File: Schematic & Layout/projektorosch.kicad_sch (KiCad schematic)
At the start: 18 parts

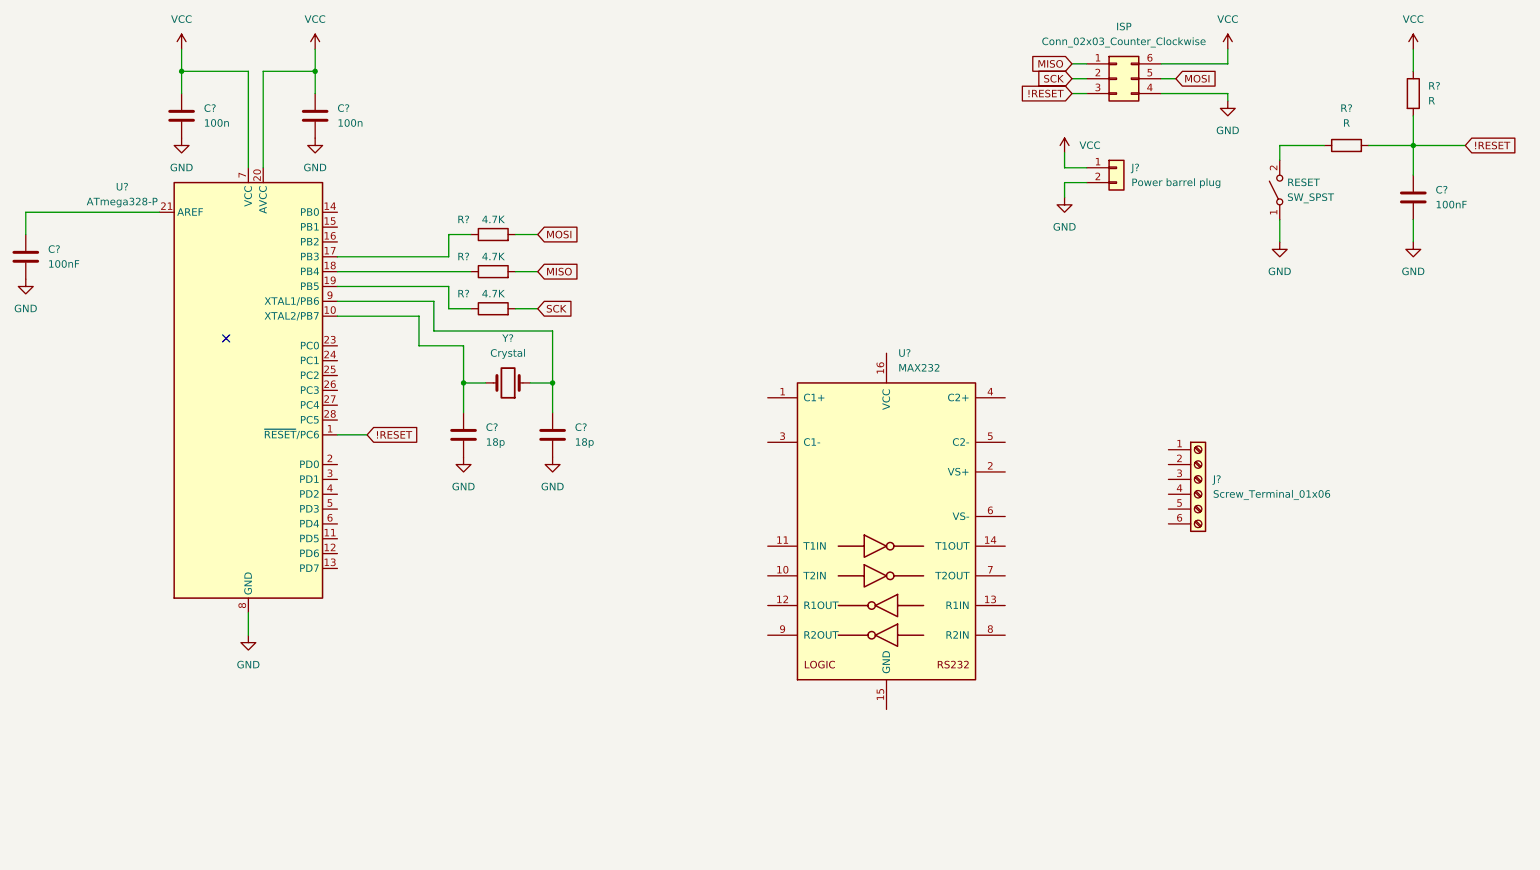
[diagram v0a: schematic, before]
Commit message: add buttons, and the connections of max232
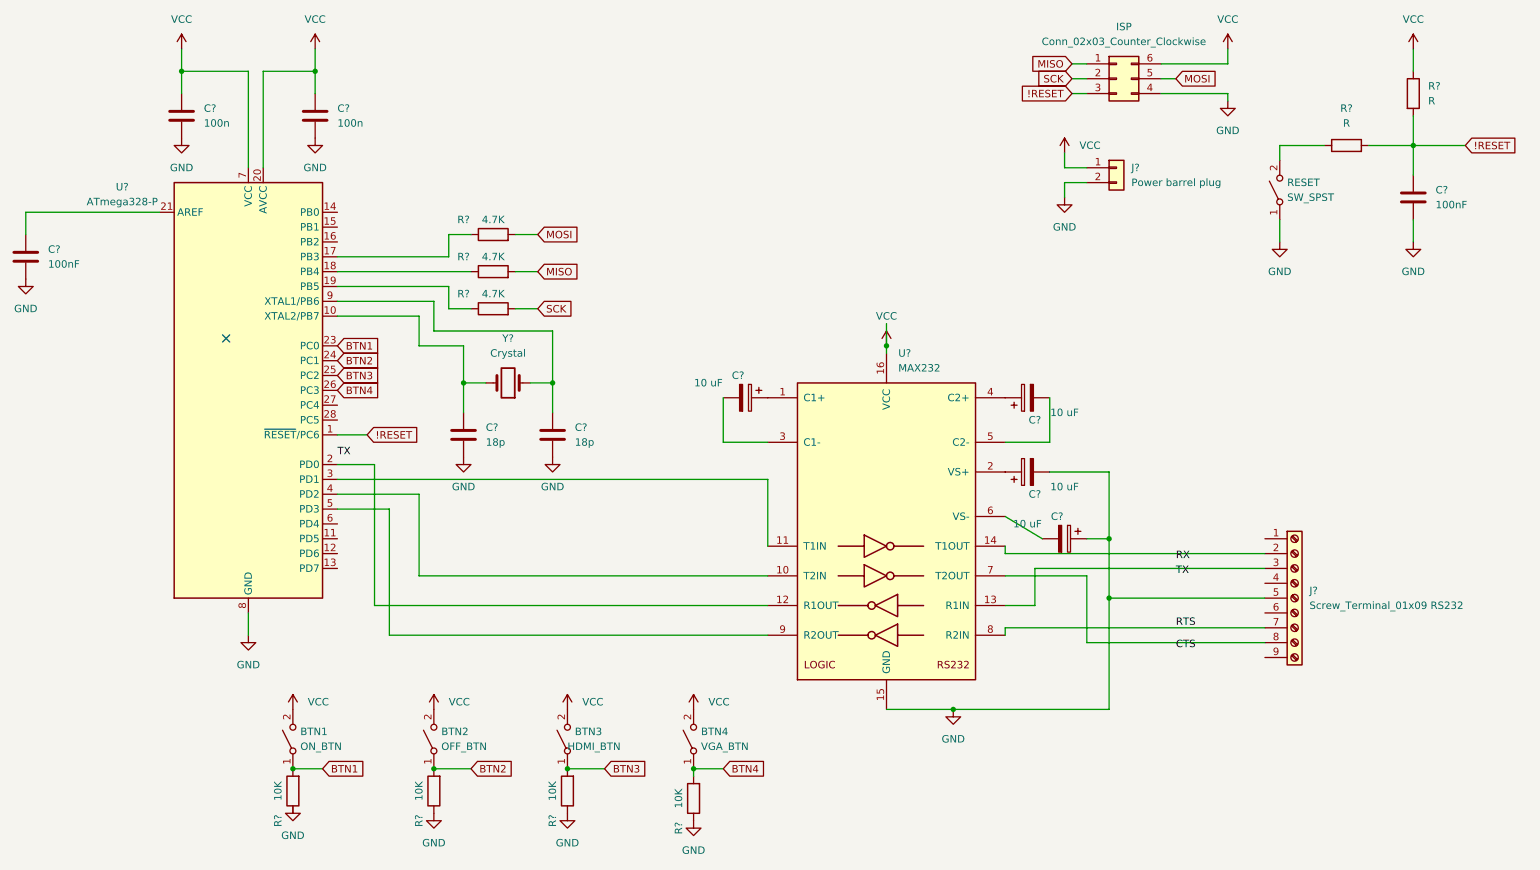
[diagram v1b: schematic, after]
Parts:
- removed J?: Screw_Terminal_01x06, Connector_Dsub:DSUB-9_Female_EdgeMount_P2.77mm, symbol Connector:Screw_Terminal_01x06
- added BTN1: ON_BTN, symbol Switch:SW_SPST
- added BTN2: OFF_BTN, symbol Switch:SW_SPST
- added BTN3: HDMI_BTN, symbol Switch:SW_SPST
- added BTN4: VGA_BTN, symbol Switch:SW_SPST
- added C? (x4): 10 uF, symbol Device:C_Polarized
- added J?: Screw_Terminal_01x09 RS232, symbol Connector:Screw_Terminal_01x09
- added R? (x4): 10K, symbol Device:R
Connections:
- net GND: now also U?.15 (GND), C?.1, C?.2, J?.5 (Pin_5), R?.1, R?.1, R?.1
- net VCC: now also U?.16 (VCC), BTN1.2 (B), BTN2.2 (B), BTN3.2 (B), BTN4.2 (B)
- net at U?.1 (C1+): now also C?.1
- net at U?.10 (T2IN): now also U?.4 (PD2)
- net at U?.11 (T1IN): now also U?.3 (PD1)
- net at U?.12 (R1OUT): now also U?.2 (PD0)
- net at U?.13 (R1IN): now also J?.3 (Pin_3)
- net at U?.14 (T1OUT): now also J?.2 (Pin_2)
- net at U?.2 (VS+): now also C?.1
- net at U?.3 (C1-): now also C?.2
- net at U?.4 (C2+): now also C?.1
- net at U?.5 (C2-): now also C?.2
- net at U?.6 (VS-): now also C?.2
- net at U?.7 (T2OUT): now also J?.8 (Pin_8)
- net RTS: now reaches U?.8 (R2IN)
- net RTS: now also J?.7 (Pin_7)
- net at U?.9 (R2OUT): now also U?.5 (PD3)
- net BTN1: now reaches U?.23 (PC0)
- net BTN1: now also BTN1.1 (A), R?.2
- net BTN2: now reaches U?.24 (PC1)
- net BTN2: now also BTN2.1 (A), R?.2
- net BTN3: now reaches U?.25 (PC2)
- net BTN3: now also BTN3.1 (A), R?.2
- net BTN4: now reaches U?.26 (PC3)
- net BTN4: now also BTN4.1 (A), R?.2

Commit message: Improvements, add overvoltage and overcurrent protection
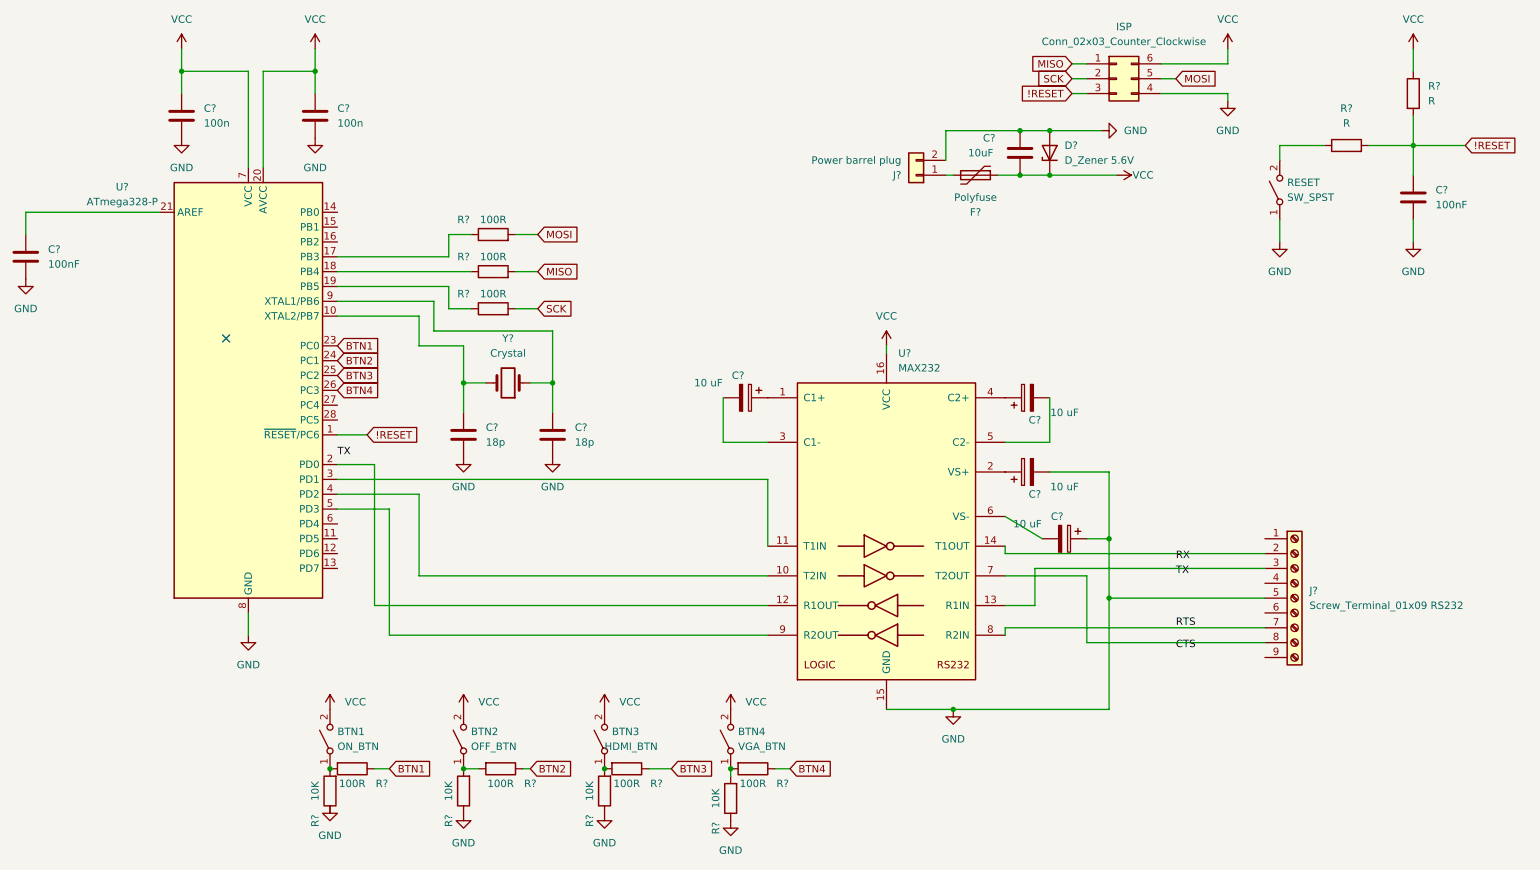
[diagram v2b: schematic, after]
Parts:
- added C?: 10uF, symbol Device:C
- added D?: D_Zener 5.6V, symbol Device:D_Zener
- added F?: Polyfuse, symbol Device:Polyfuse
- added R? (x4): 100R, symbol Device:R
- R? (x3): value 4.7K -> 100R
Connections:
- net BTN1: now also R?.1; no longer BTN1.1 (A), R?.2
- net BTN2: now also R?.1; no longer BTN2.1 (A), R?.2
- net BTN3: now also R?.1; no longer BTN3.1 (A), R?.2
- net BTN4: now also R?.1; no longer BTN4.1 (A), R?.2
- net GND: now also C?.1, D?.2 (A)
- net VCC: now also C?.2, D?.1 (K), F?.1; no longer J?.1 (Pin_1)
- new net: BTN2.1 (A), R?.2, R?.2
- new net: BTN4.1 (A), R?.2, R?.2
- new net: F?.2, J?.1 (Pin_1)
- new net: BTN1.1 (A), R?.2, R?.2
- new net: BTN3.1 (A), R?.2, R?.2
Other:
- moved on the sheet: BTN1, BTN2, BTN3, BTN4, J?, R?
